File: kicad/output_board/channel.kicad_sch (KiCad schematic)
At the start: 20 parts, among them Q4 Q_PMOS_GSD, Q5 Q_NMOS_GSD, Q6 Q_NMOS_GSD, T2 42TL004/42TU200, U2 LM358

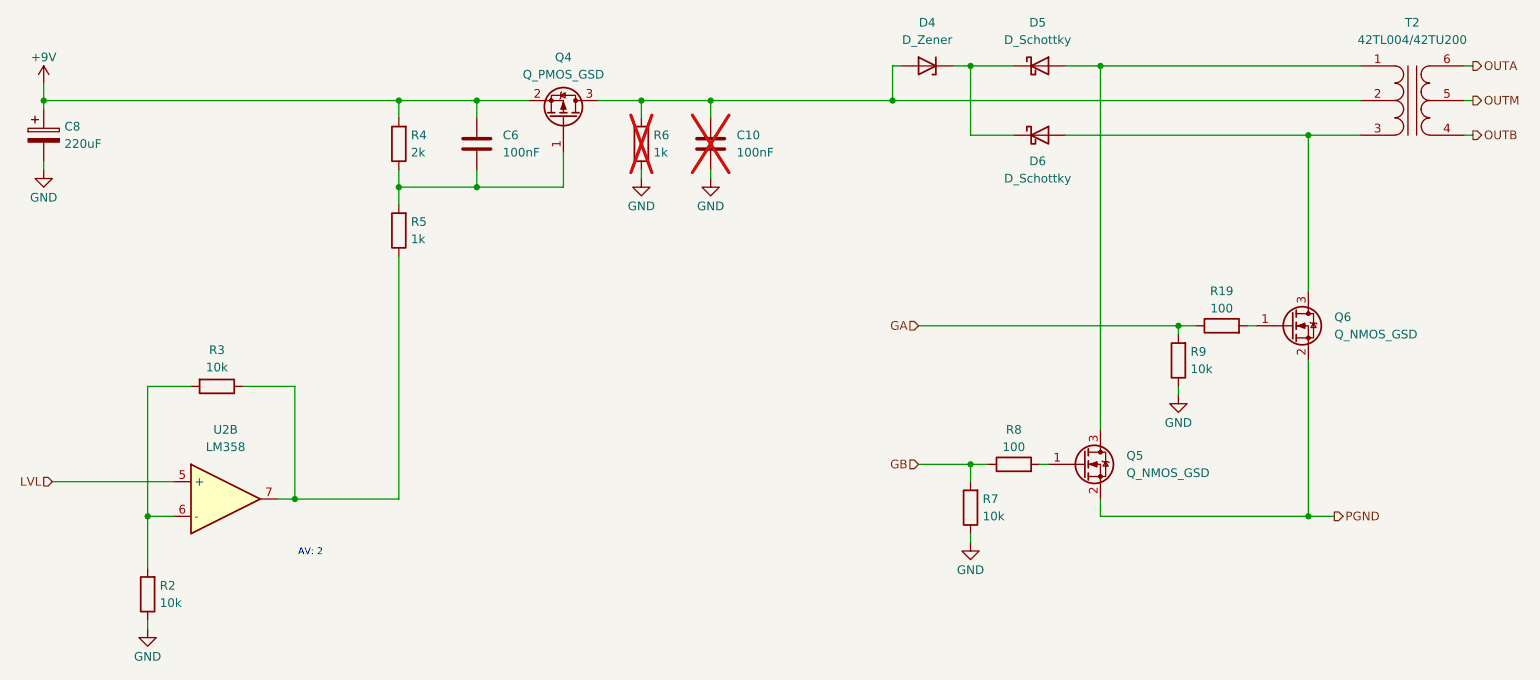
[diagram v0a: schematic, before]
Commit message: update BOM prioritizing basic parts
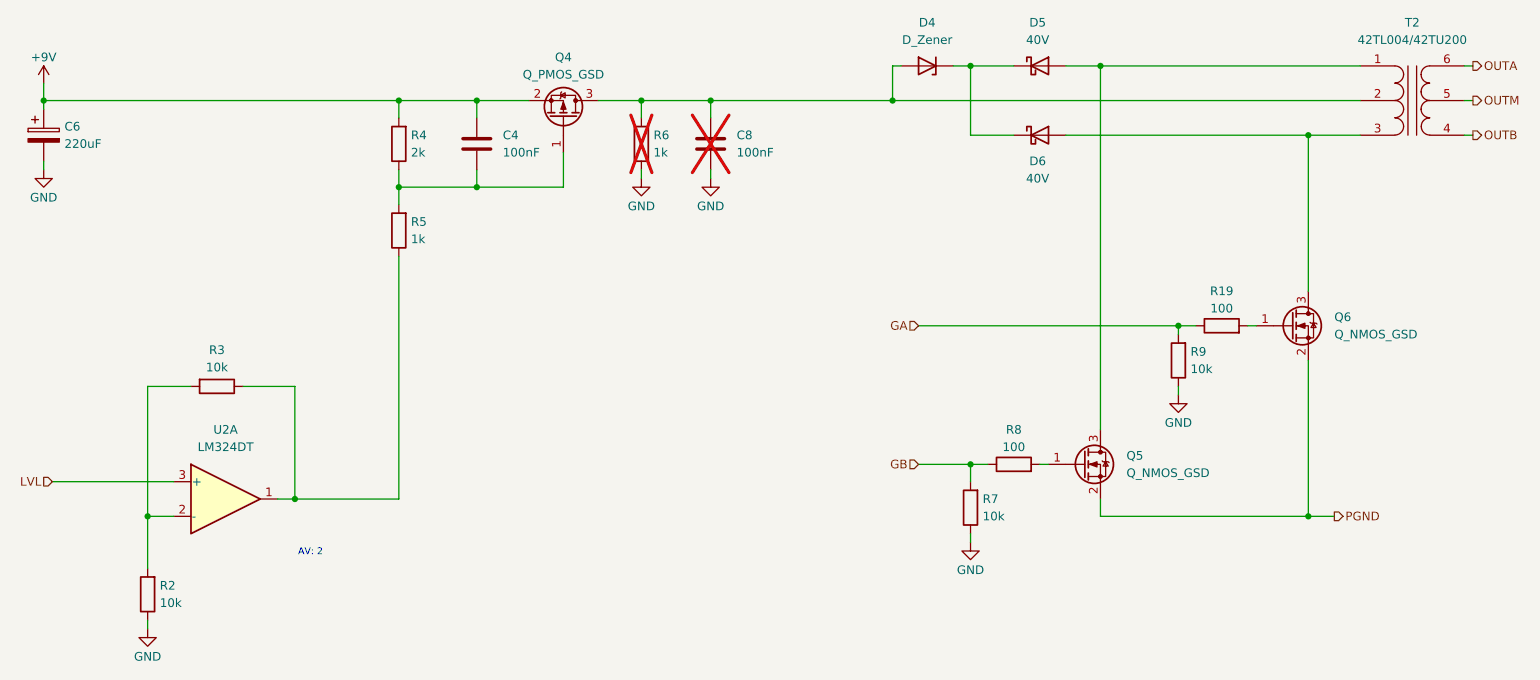
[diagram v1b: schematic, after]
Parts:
- removed U2: LM358, Package_SO:TSSOP-8_4.4x3mm_P0.65mm, symbol Device:Opamp_Dual
- added U2: LM324DT, Package_SO:SOIC-14_3.9x8.7mm_P1.27mm, symbol Amplifier_Operational:LM324
- C4: renamed from C6; JLC (none) -> C14663; LCSC C1591 -> (none); MOUSER 187-CL10B104KB8NNNC -> (none); MPN CL10B104KB8NNNC -> (none)
- C8: renamed from C10; JLC (none) -> C14663; LCSC C1591 -> (none); MOUSER 187-CL10B104KB8NNNC -> (none); MPN CL10B104KB8NNNC -> (none)
- D5, D6: value D_Schottky -> 40V; footprint (none) -> Diode_SMD:D_SOD-323; JLC (none) -> C191023
- R19, R8: JLC (none) -> C22775; LCSC C22775 -> (none); MOUSER 603-RC0603FR-13100RL -> (none); MPN RC0603FR-07100RL -> (none)
- R2, R3, R7, R9: JLC (none) -> C25804; LCSC C25804 -> (none); MOUSER 603-RC0603FR-0710KL -> (none); MPN RC0603FR-0710KL -> (none)
- R4: JLC (none) -> C17944
- R5, R6: JLC (none) -> C21190; LCSC C21190 -> (none); MOUSER 603-RC0603FR-071KL -> (none); MPN RC0603FR-071KL -> (none)
- renumbered C8 to C6
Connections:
- net LVL: now also U2.3 (+)
- net at R3.1, R5.1: now also U2.1
- net at R2.2, R3.2: now also U2.2 (-)

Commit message: add generation script
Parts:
- C4, C8: JLC C14663 -> (none); LCSC (none) -> C14663; Service (none) -> PCBA
- D4, Q4, Q5, Q6: Service (none) -> PCBA
- D5, D6: JLC C191023 -> (none); LCSC (none) -> C191023; Service (none) -> PCBA
- R19, R8: JLC C22775 -> (none); LCSC (none) -> C22775; Service (none) -> PCBA
- R2, R3, R7, R9: JLC C25804 -> (none); LCSC (none) -> C25804; Service (none) -> PCBA
- R4: JLC C17944 -> (none); LCSC (none) -> C17944; Service (none) -> PCBA
- R5, R6: JLC C21190 -> (none); LCSC (none) -> C21190; Service (none) -> PCBA
- T2: Service (none) -> HandAssembly
- U2: JLC C71035 -> (none); LCSC (none) -> C71035; Service (none) -> PCBA
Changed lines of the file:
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@@
 			)
 		)
-		(property "LCSC" ""
+		(property "LCSC" "C22775"
 			(at 218.44 96.52 0)
 			(effects
@@
 			)
 		)
-		(property "JLC" "C22775"
+		(property "Service" "PCBA"
 			(at 218.44 96.52 0)
 			(effects
@@
 			)
 		)
-		(property "LCSC" ""
+		(property "LCSC" "C21190"
 			(at 97.79 82.55 0)
 			(effects
@@
 			)
 		)
-		(property "JLC" "C21190"
+		(property "Service" "PCBA"
 			(at 97.79 82.55 0)
 			(effects
@@
 			)
 		)
-		(property "LCSC" ""
+		(property "LCSC" "C25804"
 			(at 60.96 135.89 0)
 			(effects
@@
 			)
 		)
-		(property "JLC" "C25804"
+		(property "Service" "PCBA"
 			(at 60.96 135.89 0)
 			(effects
@@
 			)
 		)
-		(property "JLC" ""
+		(property "Service" "PCBA"
 			(at 121.92 66.04 0)
 			(effects
@@
 			)
 		)
-		(property "LCSC" ""
+		(property "LCSC" "C21190"
 			(at 133.35 69.85 0)
 			(effects
@@
 			)
 		)
-		(property "JLC" "C21190"
+		(property "Service" "PCBA"
 			(at 133.35 69.85 0)
 			(effects
@@
 			)
 		)
-		(property "JLC" ""
+		(property "Service" "PCBA"
 			(at 228.6 96.52 0)
 			(effects
@@
 			)
 		)
-		(property "LCSC" ""
+		(property "LCSC" "C25804"
 			(at 181.61 123.19 0)
 			(effects
@@
 			)
 		)
-		(property "JLC" "C25804"
+		(property "Service" "PCBA"
 			(at 181.61 123.19 0)
 			(effects
@@
 			)
 		)
-		(property "JLC" ""
+		(property "Service" "HandAssembly"
 			(at 246.38 63.5 0)
 			(effects
@@
 			)
 		)
-		(property "JLC" ""
+		(property "Service" "PCBA"
 			(at 198.12 116.84 0)
 			(effects
@@
 			)
 		)
-		(property "LCSC" ""
+		(property "LCSC" "C25804"
 			(at 212.09 101.6 0)
 			(effects
@@
 			)
 		)
-		(property "JLC" "C25804"
+		(property "Service" "PCBA"
 			(at 212.09 101.6 0)
 			(effects
@@
 			)
 		)
-		(property "LCSC" ""
+		(property "LCSC" "C191023"
 			(at 191.77 58.42 0)
 			(effects
@@
 			)
 		)
-		(property "JLC" "C191023"
+		(property "Service" "PCBA"
 			(at 191.77 58.42 0)
 			(effects
@@
 			)
 		)
-		(property "LCSC" ""
+		(property "LCSC" "C25804"
 			(at 71.12 105.41 0)
 			(effects
@@
 			)
 		)
-		(property "JLC" "C25804"
+		(property "Service" "PCBA"
 			(at 71.12 105.41 0)
 			(effects
@@
 			)
 		)
-		(property "LCSC" ""
+		(property "LCSC" "C14663"
 			(at 143.51 69.85 0)
 			(effects
@@
 			)
 		)
-		(property "JLC" "C14663"
+		(property "Service" "PCBA"
 			(at 143.51 69.85 0)
 			(effects
@@
 			)
 		)
-		(property "LCSC" ""
+		(property "LCSC" "C22775"
 			(at 187.96 116.84 0)
 			(effects
@@
 			)
 		)
-		(property "JLC" "C22775"
+		(property "Service" "PCBA"
 			(at 187.96 116.84 0)
 			(effects
@@
 			)
 		)
-		(property "LCSC" ""
+		(property "LCSC" "C17944"
 			(at 97.79 69.85 0)
 			(effects
@@
 			)
 		)
-		(property "JLC" "C17944"
+		(property "Service" "PCBA"
 			(at 97.79 69.85 0)
 			(effects
@@
 			)
 		)
-		(property "JLC" ""
+		(property "Service" "PCBA"
 			(at 175.26 58.42 0)
 			(effects
@@
 			)
 		)
-		(property "JLC" ""
+		(property "Service" ""
 			(at 45.72 68.58 0)
 			(effects
@@
 			)
 		)
-		(property "LCSC" ""
+		(property "LCSC" "C14663"
 			(at 109.22 69.85 0)
 			(effects
@@
 			)
 		)
-		(property "JLC" "C14663"
+		(property "Service" "PCBA"
 			(at 109.22 69.85 0)
 			(effects
@@
 			)
 		)
-		(property "LCSC" ""
+		(property "LCSC" "C71035"
 			(at 72.39 121.92 0)
 			(effects
@@
 			)
 		)
-		(property "JLC" "C71035"
+		(property "Service" "PCBA"
 			(at 72.39 121.92 0)
 			(effects
@@
 			)
 		)
-		(property "LCSC" ""
+		(property "LCSC" "C191023"
 			(at 191.77 68.58 0)
 			(effects
@@
 			)
 		)
-		(property "JLC" "C191023"
+		(property "Service" "PCBA"
 			(at 191.77 68.58 0)
 			(effects

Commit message: add psu
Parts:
- removed D4: D_Zener, symbol Device:D_Zener
- removed D5, D6: 40V, Diode_SMD:D_SOD-323, symbol Device:D_Schottky
- removed R7, R9: 10k, Resistor_SMD:R_0603_1608Metric, symbol Device:R
- added D2: SMAJ13A, Diode_SMD:D_SMA, symbol Device:D_TVS
- added D3: BAV23CL, Package_TO_SOT_SMD:SOT-23-3, symbol Device:D_Dual_CommonCathode_AAK_Split
- added R10, R12: 100k, Resistor_SMD:R_0603_1608Metric, symbol Device:R
- C10: renamed from C6; Service (none) -> PCBA
- Q4: value Q_PMOS_GSD -> IRF9Z24NPBF; footprint Package_TO_SOT_SMD:SOT-223-3_TabPin2 -> Package_TO_SOT_THT:TO-220-3_Vertical; symbol Device:Q_PMOS_GSD -> Device:Q_PMOS_GDS; LCSC (none) -> C2576
- T2: footprint (none) -> SaawLib:42TL_TU
- renumbered C8 to C12, C4 to C8, R8 to R11, R19 to R22, R2 to R5, R3 to R6, R4 to R7, R5 to R8, R6 to R9
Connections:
- net +9V: now also Q4.3 (S), D2.2 (A2); no longer Q4.2 (S)
- net GA: now also R12.1
- net GB: now also R10.1
- net GND: now also R10.2, R12.2
- net at C12.1, R9.2, T2.2 (PM): now also Q4.2 (D); no longer Q4.3 (D)
- net at Q6.3 (D), T2.3 (PR2): now also D3.2 (K)
- net at Q5.3 (D), T2.1 (PR1): now also D3.1 (A)
- new net: D2.1 (A1), D3.3 (K), D3.3 (K)

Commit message: update bom
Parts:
- Q4: Service PCBA -> HandAssembly
- Q5, Q6: value Q_NMOS_GSD -> AO3400A; LCSC (none) -> C20917
- R7: LCSC C17944 -> C22975
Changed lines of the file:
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@@
 			)
 		)
-		(property "Datasheet" "~"
+		(property "Datasheet" "https://www.lcsc.com/datasheet/lcsc_datasheet_1809192211_Infineon-Technologies-IRF9Z24NPBF_C2576.pdf"
 			(at 121.92 66.04 0)
 			(effects
@@
 			)
 		)
-		(property "Service" "PCBA"
+		(property "Service" "HandAssembly"
 			(at 121.92 66.04 0)
 			(effects
@@
 			)
 		)
-		(property "Value" "Q_NMOS_GSD"
+		(property "Value" "AO3400A"
 			(at 234.95 97.7899 0)
 			(effects
@@
 			)
 		)
-		(property "Datasheet" "~"
+		(property "Datasheet" "https://www.lcsc.com/datasheet/lcsc_datasheet_1811081213_Alpha---Omega-Semicon-AO3400A_C20917.pdf"
 			(at 228.6 96.52 0)
 			(effects
@@
 		)
 		(property "Service" "PCBA"
+			(at 228.6 96.52 0)
+			(effects
+				(font
+					(size 1.27 1.27)
+				)
+				(hide yes)
+			)
+		)
+		(property "LCSC" "C20917"
 			(at 228.6 96.52 0)
 			(effects
@@
 			)
 		)
-		(property "Datasheet" ""
+		(property "Datasheet" "https://www.mouser.com/datasheet/2/449/Yuetone_XC-600127-1212403.pdf"
 			(at 246.38 63.5 0)
 			(effects
@@
 			)
 		)
-		(property "Value" "Q_NMOS_GSD"
+		(property "Value" "AO3400A"
 			(at 204.47 118.1099 0)
 			(effects
@@
 			)
 		)
-		(property "Datasheet" "~"
+		(property "Datasheet" "https://www.lcsc.com/datasheet/lcsc_datasheet_1811081213_Alpha---Omega-Semicon-AO3400A_C20917.pdf"
 			(at 198.12 116.84 0)
 			(effects
@@
 		)
 		(property "Service" "PCBA"
+			(at 198.12 116.84 0)
+			(effects
+				(font
+					(size 1.27 1.27)
+				)
+				(hide yes)
+			)
+		)
+		(property "LCSC" "C20917"
 			(at 198.12 116.84 0)
 			(effects
@@
 			)
 		)
-		(property "Datasheet" "~"
+		(property "Datasheet" "https://www.lcsc.com/datasheet/lcsc_datasheet_2304140030_Diodes-Incorporated-SMAJ13A-13-F_C110519.pdf"
 			(at 175.26 58.42 0)
 			(effects
@@
 			)
 		)
-		(property "Datasheet" "~"
+		(property "Datasheet" "https://www.lcsc.com/datasheet/lcsc_datasheet_2210210130_onsemi-BAV23CLT1G_C232533.pdf"
 			(at 194.31 55.88 0)
 			(effects
@@
 			)
 		)
-		(property "Datasheet" "https://www.lcsc.com/datasheet/lcsc_datasheet_2206010145_UNI-ROYAL-Uniroyal-Elec-1206W4F2001T5E_C17944.pdf"
+		(property "Datasheet" "https://www.lcsc.com/datasheet/lcsc_datasheet_2206010116_UNI-ROYAL-Uniroyal-Elec-0603WAF2001T5E_C22975.pdf"
 			(at 97.79 69.85 0)
 			(effects
@@
 			)
 		)
-		(property "LCSC" "C17944"
+		(property "LCSC" "C22975"
 			(at 97.79 69.85 0)
 			(effects
@@
 			)
 		)
-		(property "Datasheet" "~"
+		(property "Datasheet" "https://www.lcsc.com/datasheet/lcsc_datasheet_2210210130_onsemi-BAV23CLT1G_C232533.pdf"
 			(at 194.31 66.04 0)
 			(effects
